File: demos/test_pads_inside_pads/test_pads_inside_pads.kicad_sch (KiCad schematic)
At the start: 4 parts, among them P1 CONN_1, P2 CONN_1, P3 CONN_1, P4 CONN_1

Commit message: Demos update
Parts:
- U: renamed from P2; value CONN_1 -> (none); footprint Connect:1pin -> (none)
- U: renamed from P1; value CONN_1 -> (none); footprint Connect:1pin -> (none)
- U: renamed from P3; value CONN_1 -> (none); footprint Connect:1pin -> (none)
- U: renamed from P4; value CONN_1 -> (none); footprint Connect:1pin -> (none)
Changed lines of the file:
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@@
-(kicad_sch (version 20210406) (generator eeschema)
+(kicad_sch (version 20220404) (generator eeschema)
   (paper "A4")
   (title_block
@@
   )
   (wire (pts (xy 105.41 36.83) (xy 95.25 36.83))
-    (stroke (width 0) (type solid) (color 0 0 0 0))
+    (stroke (width 0) (type solid))
   )
   (wire (pts (xy 105.41 44.45) (xy 95.25 44.45))
-    (stroke (width 0) (type solid) (color 0 0 0 0))
+    (stroke (width 0) (type solid))
   )
-  (label "NET1" (at 97.79 36.83 0)
+  (label "NET2" (at 97.79 44.45 0) (fields_autoplaced)
     (effects (font (size 1.524 1.524)) (justify left bottom))
   )
-  (label "NET2" (at 97.79 44.45 0)
+  (label "NET1" (at 97.79 36.83 0) (fields_autoplaced)
     (effects (font (size 1.524 1.524)) (justify left bottom))
+  )
+  (symbol (lib_id "test_pads_inside_pads_schlib:CONN_1") (at 109.22 44.45 0) (unit 1)
+    (in_bom yes) (on_board yes)
+    (default_instance (reference "U") (unit 1) (value "") (footprint ""))
+    (property "Reference" "U" (id 0) (at 111.252 44.45 0)
+      (effects (font (size 1.016 1.016)) (justify left))
+    )
+    (property "Value" "" (id 1) (at 109.22 43.053 0)
+      (effects (font (size 0.762 0.762)) hide)
+    )
+    (property "Footprint" "" (id 2) (at 109.22 45.72 0)
+      (effects (font (size 0.762 0.762)))
+    )
+    (property "Datasheet" "" (id 3) (at 109.22 44.45 0)
+      (effects (font (size 1.524 1.524)) hide)
+    )
+    (pin "1")
+  )
+  (symbol (lib_id "test_pads_inside_pads_schlib:CONN_1") (at 91.44 44.45 180) (unit 1)
+    (in_bom yes) (on_board yes)
+    (default_instance (reference "U") (unit 1) (value "") (footprint ""))
+    (property "Reference" "U" (id 0) (at 89.408 44.45 0)
+      (effects (font (size 1.016 1.016)) (justify left))
+    )
+    (property "Value" "" (id 1) (at 91.44 45.847 0)
+      (effects (font (size 0.762 0.762)) hide)
+    )
+    (property "Footprint" "" (id 2) (at 91.44 45.72 0)
+      (effects (font (size 0.762 0.762)))
+    )
+    (property "Datasheet" "" (id 3) (at 91.44 44.45 0)
+      (effects (font (size 1.524 1.524)) hide)
+    )
+    (pin "1")
   )
   (symbol (lib_id "test_pads_inside_pads_schlib:CONN_1") (at 91.44 36.83 180) (unit 1)
     (in_bom yes) (on_board yes)
-    (property "Reference" "P3" (id 0) (at 89.408 36.83 0)
+    (default_instance (reference "U") (unit 1) (value "") (footprint ""))
+    (property "Reference" "U" (id 0) (at 89.408 36.83 0)
       (effects (font (size 1.016 1.016)) (justify left))
     )
-    (property "Value" "CONN_1" (id 1) (at 91.44 38.227 0)
+    (property "Value" "" (id 1) (at 91.44 38.227 0)
       (effects (font (size 0.762 0.762)) hide)
     )
-    (property "Footprint" "Connect:1pin" (id 2) (at 91.44 38.1 0)
-      (effects (font (size 1.524 1.524)))
+    (property "Footprint" "" (id 2) (at 91.44 38.1 0)
+      (effects (font (size 0.762 0.762)))
     )
     (property "Datasheet" "" (id 3) (at 91.44 36.83 0)
@@
     (pin "1")
   )
-  (symbol (lib_id "test_pads_inside_pads_schlib:CONN_1") (at 91.44 44.45 180) (unit 1)
+  (symbol (lib_id "test_pads_inside_pads_schlib:CONN_1") (at 109.22 36.83 0) (unit 1)
     (in_bom yes) (on_board yes)
-    (property "Reference" "P1" (id 0) (at 89.408 44.45 0)
+    (default_instance (reference "U") (unit 1) (value "") (footprint ""))
+    (property "Reference" "U" (id 0) (at 111.252 36.83 0)
       (effects (font (size 1.016 1.016)) (justify left))
     )
-    (property "Value" "CONN_1" (id 1) (at 91.44 45.847 0)
+    (property "Value" "" (id 1) (at 109.22 35.433 0)
       (effects (font (size 0.762 0.762)) hide)
     )
-    (property "Footprint" "Connect:1pin" (id 2) (at 91.44 45.72 0)
-      (effects (font (size 1.524 1.524)))
-    )
-    (property "Datasheet" "" (id 3) (at 91.44 44.45 0)
-      (effects (font (size 1.524 1.524)) hide)
-    )
-    (pin "1")
-  )
-  (symbol (lib_id "test_pads_inside_pads_schlib:CONN_1") (at 109.22 36.83 0) (unit 1)
-    (in_bom yes) (on_board yes)
-    (property "Reference" "P4" (id 0) (at 111.252 36.83 0)
-      (effects (font (size 1.016 1.016)) (justify left))
-    )
-    (property "Value" "CONN_1" (id 1) (at 109.22 35.433 0)
-      (effects (font (size 0.762 0.762)) hide)
-    )
-    (property "Footprint" "Connect:1pin" (id 2) (at 109.22 38.1 0)
-      (effects (font (size 1.524 1.524)))
+    (property "Footprint" "" (id 2) (at 109.22 38.1 0)
+      (effects (font (size 0.762 0.762)))
     )
     (property "Datasheet" "" (id 3) (at 109.22 36.83 0)
-      (effects (font (size 1.524 1.524)) hide)
-    )
-    (pin "1")
-  )
-  (symbol (lib_id "test_pads_inside_pads_schlib:CONN_1") (at 109.22 44.45 0) (unit 1)
-    (in_bom yes) (on_board yes)
-    (property "Reference" "P2" (id 0) (at 111.252 44.45 0)
-      (effects (font (size 1.016 1.016)) (justify left))
-    )
-    (property "Value" "CONN_1" (id 1) (at 109.22 43.053 0)
-      (effects (font (size 0.762 0.762)) hide)
-    )
-    (property "Footprint" "Connect:1pin" (id 2) (at 109.22 45.72 0)
-      (effects (font (size 1.524 1.524)))
-    )
-    (property "Datasheet" "" (id 3) (at 109.22 44.45 0)
       (effects (font (size 1.524 1.524)) hide)
     )
@@
   (symbol_instances
     (path "/00000000-0000-0000-0000-00004edf7cc5"
-      (reference "P1") (unit 1) (value "CONN_1") (footprint "Connect:1pin")
+      (reference "P1") (unit 1) (value "CONN_1") (footprint "Connect:1pin_thermal")
     )
     (path "/00000000-0000-0000-0000-00004edf7cc0"

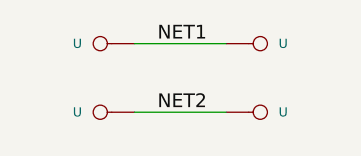
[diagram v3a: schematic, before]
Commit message: Update demos using latest file formats.
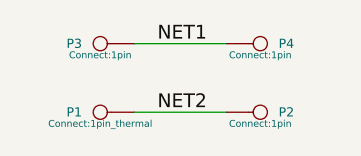
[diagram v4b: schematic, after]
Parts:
- P1: renamed from U; value (none) -> CONN_1; footprint (none) -> Connect:1pin_thermal
- P2, P3, P4: renamed from U; value (none) -> CONN_1; footprint (none) -> Connect:1pin
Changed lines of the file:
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@@
-(kicad_sch (version 20220404) (generator eeschema)
+(kicad_sch (version 20230121) (generator eeschema)
   (paper "A4")
   (title_block
@@
   )
   (symbol (lib_id "test_pads_inside_pads_schlib:CONN_1") (at 109.22 44.45 0) (unit 1)
-    (in_bom yes) (on_board yes)
-    (default_instance (reference "U") (unit 1) (value "") (footprint ""))
-    (property "Reference" "U" (id 0) (at 111.252 44.45 0)
+    (in_bom yes) (on_board yes) (dnp no)
+    (property "Reference" "P2" (at 111.252 44.45 0)
       (effects (font (size 1.016 1.016)) (justify left))
     )
-    (property "Value" "" (id 1) (at 109.22 43.053 0)
+    (property "Value" "CONN_1" (at 109.22 43.053 0)
       (effects (font (size 0.762 0.762)) hide)
     )
-    (property "Footprint" "" (id 2) (at 109.22 45.72 0)
+    (property "Footprint" "Connect:1pin" (at 109.22 45.72 0)
       (effects (font (size 0.762 0.762)))
     )
-    (property "Datasheet" "" (id 3) (at 109.22 44.45 0)
+    (property "Datasheet" "" (at 109.22 44.45 0)
       (effects (font (size 1.524 1.524)) hide)
     )
     (pin "1")
+    (instances
+      (project "test_pads_inside_pads"
+        (path "/8d3a5066-9577-4e18-8fe9-905c643339bb"
+          (reference "P2") (unit 1)
+        )
+      )
+    )
   )
   (symbol (lib_id "test_pads_inside_pads_schlib:CONN_1") (at 91.44 44.45 180) (unit 1)
-    (in_bom yes) (on_board yes)
-    (default_instance (reference "U") (unit 1) (value "") (footprint ""))
-    (property "Reference" "U" (id 0) (at 89.408 44.45 0)
+    (in_bom yes) (on_board yes) (dnp no)
+    (property "Reference" "P1" (at 89.408 44.45 0)
       (effects (font (size 1.016 1.016)) (justify left))
     )
-    (property "Value" "" (id 1) (at 91.44 45.847 0)
+    (property "Value" "CONN_1" (at 91.44 45.847 0)
       (effects (font (size 0.762 0.762)) hide)
     )
-    (property "Footprint" "" (id 2) (at 91.44 45.72 0)
+    (property "Footprint" "Connect:1pin_thermal" (at 91.44 45.72 0)
       (effects (font (size 0.762 0.762)))
     )
-    (property "Datasheet" "" (id 3) (at 91.44 44.45 0)
+    (property "Datasheet" "" (at 91.44 44.45 0)
       (effects (font (size 1.524 1.524)) hide)
     )
     (pin "1")
+    (instances
+      (project "test_pads_inside_pads"
+        (path "/8d3a5066-9577-4e18-8fe9-905c643339bb"
+          (reference "P1") (unit 1)
+        )
+      )
+    )
   )
   (symbol (lib_id "test_pads_inside_pads_schlib:CONN_1") (at 91.44 36.83 180) (unit 1)
-    (in_bom yes) (on_board yes)
-    (default_instance (reference "U") (unit 1) (value "") (footprint ""))
-    (property "Reference" "U" (id 0) (at 89.408 36.83 0)
+    (in_bom yes) (on_board yes) (dnp no)
+    (property "Reference" "P3" (at 89.408 36.83 0)
       (effects (font (size 1.016 1.016)) (justify left))
     )
-    (property "Value" "" (id 1) (at 91.44 38.227 0)
+    (property "Value" "CONN_1" (at 91.44 38.227 0)
       (effects (font (size 0.762 0.762)) hide)
     )
-    (property "Footprint" "" (id 2) (at 91.44 38.1 0)
+    (property "Footprint" "Connect:1pin" (at 91.44 38.1 0)
       (effects (font (size 0.762 0.762)))
     )
-    (property "Datasheet" "" (id 3) (at 91.44 36.83 0)
+    (property "Datasheet" "" (at 91.44 36.83 0)
       (effects (font (size 1.524 1.524)) hide)
     )
     (pin "1")
+    (instances
+      (project "test_pads_inside_pads"
+        (path "/8d3a5066-9577-4e18-8fe9-905c643339bb"
+          (reference "P3") (unit 1)
+        )
+      )
+    )
   )
   (symbol (lib_id "test_pads_inside_pads_schlib:CONN_1") (at 109.22 36.83 0) (unit 1)
-    (in_bom yes) (on_board yes)
-    (default_instance (reference "U") (unit 1) (value "") (footprint ""))
-    (property "Reference" "U" (id 0) (at 111.252 36.83 0)
+    (in_bom yes) (on_board yes) (dnp no)
+    (property "Reference" "P4" (at 111.252 36.83 0)
       (effects (font (size 1.016 1.016)) (justify left))
     )
-    (property "Value" "" (id 1) (at 109.22 35.433 0)
+    (property "Value" "CONN_1" (at 109.22 35.433 0)
       (effects (font (size 0.762 0.762)) hide)
     )
-    (property "Footprint" "" (id 2) (at 109.22 38.1 0)
+    (property "Footprint" "Connect:1pin" (at 109.22 38.1 0)
       (effects (font (size 0.762 0.762)))
     )
-    (property "Datasheet" "" (id 3) (at 109.22 36.83 0)
+    (property "Datasheet" "" (at 109.22 36.83 0)
       (effects (font (size 1.524 1.524)) hide)
     )
     (pin "1")
+    (instances
+      (project "test_pads_inside_pads"
+        (path "/8d3a5066-9577-4e18-8fe9-905c643339bb"
+          (reference "P4") (unit 1)
+        )
+      )
+    )
   )
   (sheet_instances
     (path "/" (page "1"))
   )
-  (symbol_instances
-    (path "/00000000-0000-0000-0000-00004edf7cc5"
-      (reference "P1") (unit 1) (value "CONN_1") (footprint "Connect:1pin_thermal")
-    )
-    (path "/00000000-0000-0000-0000-00004edf7cc0"
-      (reference "P2") (unit 1) (value "CONN_1") (footprint "Connect:1pin")
-    )
-    (path "/00000000-0000-0000-0000-00004ee5056c"
-      (reference "P3") (unit 1) (value "CONN_1") (footprint "Connect:1pin")
-    )
-    (path "/00000000-0000-0000-0000-00004ee5056d"
-      (reference "P4") (unit 1) (value "CONN_1") (footprint "Connect:1pin")
-    )
-  )
 )
